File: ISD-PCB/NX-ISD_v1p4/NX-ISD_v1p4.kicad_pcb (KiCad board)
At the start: 4 copper layers, 77 x 48.6 mm, 114 parts, among them J1 UJ20-C-H-G-SMT-1-P16-TR, J2 1-2328702-0, J3 1051620001, P1 S2B-PH-SM4-TB, Q1 BC847W, Q2 AO3401A, Q3 AO3400A, Q4 AO3400A, U1 RT9193-18GB, U10 OPT3001DNPR, U11 BNO085, U12 RV-3028-C7, U13 ESP32-S3-WROOM-1-N16R8, U2 USBLC6-2P6, U3 TLV62568DBV, U5 BQ25170DSGR, U6 MAX17048G_T10, U7 BME690, U8 MAX30102, U9 PCA9306, Y1 32.768 kHz

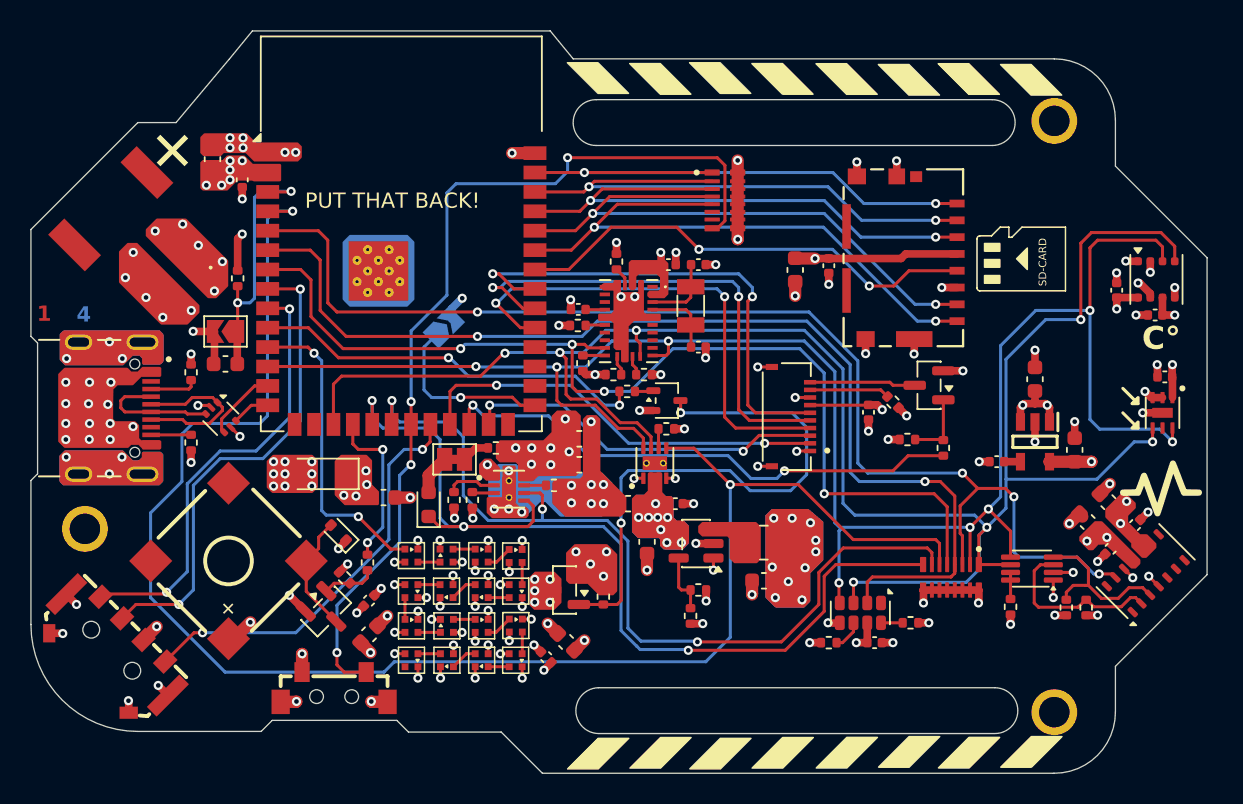
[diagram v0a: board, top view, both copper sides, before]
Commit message: hw(v1p4): add RTC backup supercap C27, tactile buttons, USBLC6 footprint adjustments, and cyberpunk silkscreens
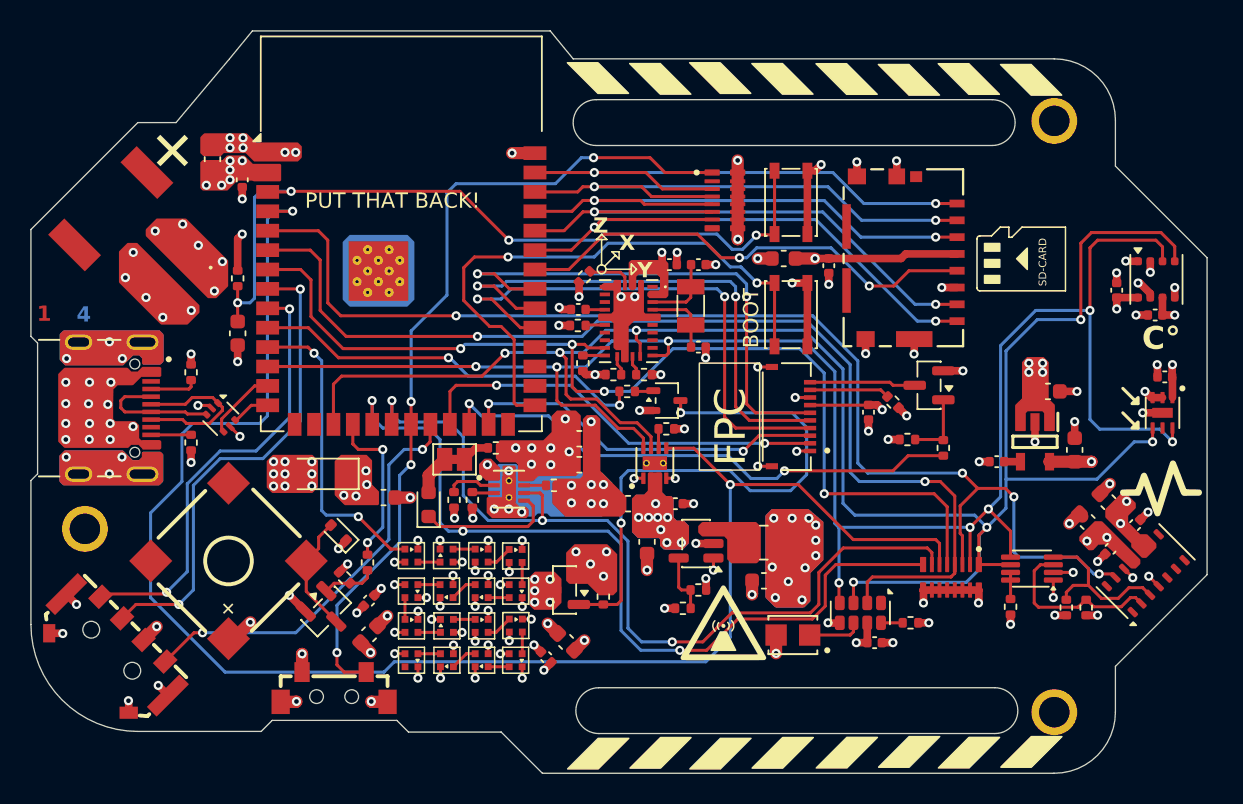
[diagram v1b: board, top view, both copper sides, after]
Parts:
- removed JP2: RESET, Jumper:SolderJumper-2_P1.3mm_Open_TrianglePad1.0x1.5mm
- removed JP3: BOOT, Jumper:SolderJumper-2_P1.3mm_Open_TrianglePad1.0x1.5mm
- removed R28: 10k, Resistor_SMD:R_0402_1005Metric
- added C5: CPH3225A, NX-AW-footprints:CAPCP3225X100N, F.Cu at (162.2, 117.7)
- added G***: LOGO, NX-ISD_silkscreen designs:emc-warning, F.Cu at (157.7, 116.8)
- added SW1: BOOT, Button_Switch_SMD:SW_SPST_PTS810, F.Cu at (162.1, 96.7)
- added SW2: RST, Button_Switch_SMD:SW_SPST_PTS810, F.Cu at (162.1, 89.3)
- added XYZ: n/a, NX-ISD_silkscreen designs:XYZ_DOF_symbol, F.Cu at (150.7, 92.8)
- R6: value 604 -> 499
- moved R13 2.33 mm to (148.6, 94.2), turned to -135 degrees
- moved C26 2.15 mm to (125.9, 97.9), turned to -90 degrees
- moved C1 1.17 mm to (178.9, 101.7), turned to 0 degrees
- moved C27 1.06 mm to (161.7, 93.0), turned to 180 degrees
- moved R3 0.71 mm to (155.1, 115.9), turned to 180 degrees
- moved C19 0.07 mm to (154.2, 93.4)
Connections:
- RN2 pad 1: /Logic section/SD_DAT2 -> /Logic section/BTN
- RN2 pad 2: /Logic section/CS_SD -> unconnected-(RN2-Pad2)
- RN2 pad 3: /Logic section/SD_CMD -> /Logic section/SD_DAT2
- RN2 pad 4: /Logic section/SD_DAT0 -> /Logic section/CS_SD
- RN2 pad 5: /Logic section/SD_DAT1 -> /Logic section/SD_CMD
- RN2 pad 6: unconnected-(RN2-Pad6) -> /Logic section/SD_DAT0
- RN2 pad 7: unconnected-(RN2-Pad7) -> /Logic section/SD_DAT1
- RN2 pad 8: /Logic section/BTN -> unconnected-(RN2-Pad8)
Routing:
- net /Logic section/EN: track 17.2 -> 52.4 mm, vias 2 -> 4
- net /Logic section/BOOT: track 11.6 -> 38.3 mm, vias 1 -> 2
- net GND: track 80.9 -> 87.8 mm, vias 120 -> 121
- net /Logic section/BTN: track 60.6 -> 55.1 mm
- net +3V3: track 52.0 -> 47.2 mm, vias 42 -> 45
- net /Logic section/SCK: track 32.6 -> 35.0 mm
- net /Logic section/MOSI: track 32.9 -> 34.9 mm
- net Net-(U11-~{BOOT}): track 1.31 -> 3.03 mm
- net /Logic section/RST: track 32.7 -> 34.3 mm
- net Net-(U12-VBACKUP): track 2.00 -> 3.65 mm
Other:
- board text added: "BOOT"
- board text added: "INTELLIGENT SENSOR DEVICE"
- board text added: "NX-ISD"
- board text removed: "NX-ISD INTELLIGENT SENSOR DEVICE"
- board text removed: "RST"
